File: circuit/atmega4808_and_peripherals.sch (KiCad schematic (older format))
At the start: 30 parts, among them J3 Conn_01x04, J4 Conn_02x04_Top_Bottom, J5 Conn_02x04_Top_Bottom, Q1 BSS138, U10 ATmega4808-X, U7 SN65HVD72, U8 TC4424AVOA, U9 ESP32-WROOM-32

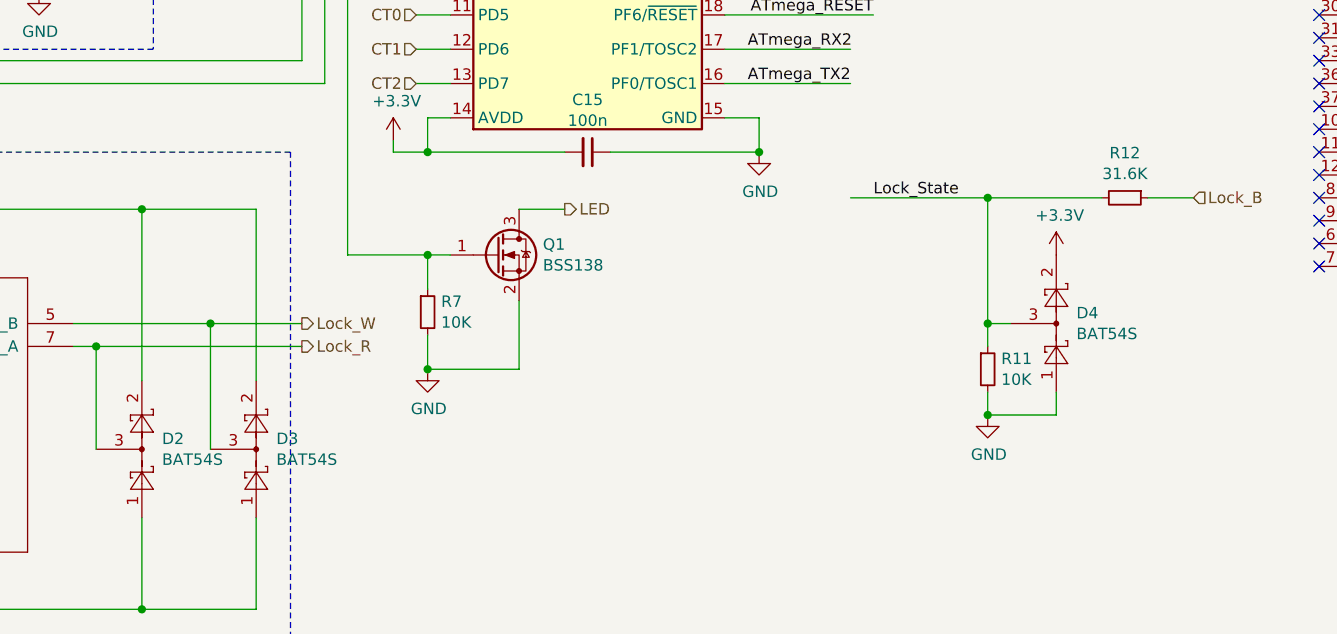
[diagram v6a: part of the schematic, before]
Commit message: Add new component data in schematic
Updated components and footprints in schematic
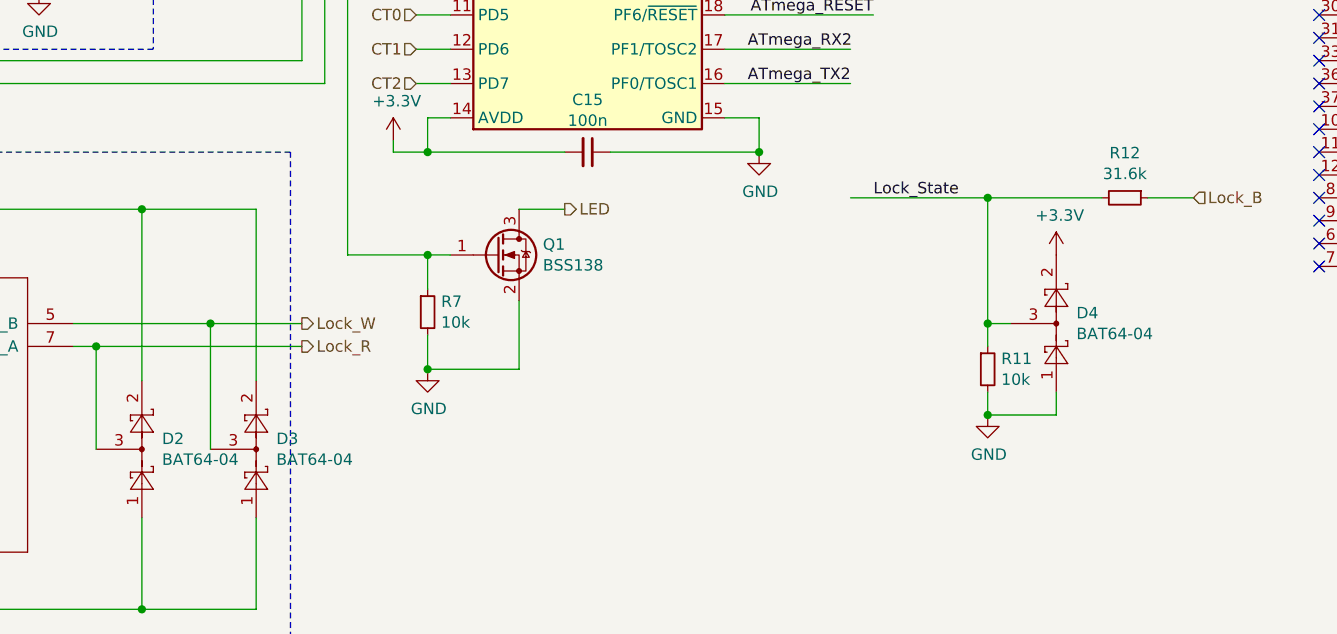
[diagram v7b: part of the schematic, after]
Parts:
- C12: footprint (none) -> Capacitor_THT:CP_Radial_D22.0mm_P10.00mm_SnapIn; Part (none) -> Yageo LG016M10K0BPF-2230 Elektrolyt-Kondensator SnapIn 10 m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; PartNo (none) -> 445516; Supplier (none) -> Conrad
- C13, C14, C15, C17: footprint (none) -> Capacitor_SMD:C_0603_1608Metric_Pad1.05x0.95mm_HandSolder; Part (none) -> Kemet C0603C104K3RAC7867+ Keramik-Kondensator SMD 0603 100 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; PartNo (none) -> 1420339; Supplier (none) -> Conrad
- C16: footprint (none) -> Capacitor_Tantalum_SMD:CP_EIA-7343-15_Kemet-W_Pad2.25x2.55mm_HandSolder; Part (none) -> Kemet T491D107K010AT Tantal-Kondensator SMD 100 µF 10 V 10 %; PartNo (none) -> 458352; Supplier (none) -> Conrad
- C21: footprint (none) -> Capacitor_SMD:C_0603_1608Metric_Pad1.05x0.95mm_HandSolder; Part (none) -> Thomsen Keramik-Kondensator SMD 0603 1 nF 50 V 10 %; PartNo (none) -> 454419; Supplier (none) -> Conrad
- C22: footprint (none) -> Capacitor_SMD:C_0603_1608Metric_Pad1.05x0.95mm_HandSolder; Part (none) -> Kemet C0603C105K4PAC7867+ Keramik-Kondensator SMD 0603 1 µF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; PartNo (none) -> 457925; Supplier (none) -> Conrad
- D2, D3, D4: value BAT54S -> BAT64-04; footprint Package_TO_SOT_SMD:SOT-23 -> Package_TO_SOT_SMD:SOT-23_Handsoldering; Part (none) -> Gleichrichter BAT64-04 (Dual) SOT-23-3 40 V Array - 1 Paar 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; PartNo (none) -> 152998; Supplier (none) -> Conrad
- J3: Part (none) -> BKL Electronic Stiftleiste (Standard) Anzahl Reihen: 1 Polz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; PartNo (none) -> 741146; Supplier (none) -> Conrad
- J4, J5: Part (none) -> econ connect SL8G2 Stiftleisten; PartNo (none) -> 801093043
- Q1: footprint (none) -> Package_TO_SOT_SMD:SOT-23_Handsoldering; Part (none) -> Infineon Technologies BSS138 MOSFET 1 N-Kanal 360 mW SOT-23; PartNo (none) -> 152928; Supplier (none) -> Conrad
- R10, R3, R4, R5, R6, R8, R9: footprint (none) -> Resistor_SMD:R_0603_1608Metric_Pad1.05x0.95mm_HandSolder; Part (none) -> TRU COMPONENTS TC-0603SAJ0101T5E203 Dickschicht-Widerstand 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; PartNo (none) -> 1583838; Supplier (none) -> Conrad
- R11, R7: value 10K -> 10k; footprint (none) -> Resistor_SMD:R_0603_1608Metric_Pad1.05x0.95mm_HandSolder; Part (none) -> TRU COMPONENTS TC-0603SAF1002T5E203 Dickschicht-Widerstand 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; PartNo (none) -> 1585269; Supplier (none) -> Conrad
- R12: value 31.6K -> 31.6k; footprint (none) -> Resistor_SMD:R_0603_1608Metric_Pad1.05x0.95mm_HandSolder; Part (none) -> TRU COMPONENTS TC-0603SAJ0303T5E203 Dickschicht-Widerstand 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; PartNo (none) -> 1584281; Supplier (none) -> Conrad
- R25: footprint (none) -> Resistor_SMD:R_0603_1608Metric_Pad1.05x0.95mm_HandSolder; Part (none) -> TRU COMPONENTS TC-0603SAJ0123T5E203 Dickschicht-Widerstand 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; PartNo (none) -> 1585796; Supplier (none) -> Conrad

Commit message: Update Parts List with Mouser ordering info
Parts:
- C12: Part Yageo LG016M10K0BPF-2230 Elektrolyt-Kondensator SnapIn 10 m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 -> (none); PartNo 445516 -> (none); Supplier Conrad -> Mouser
- C13, C14, C15, C17: Part Kemet C0603C104K3RAC7867+ Keramik-Kondensator SMD 0603 100 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 -> (none); PartNo 1420339 -> (none); Supplier Conrad -> Mouser
- C16: Part Kemet T491D107K010AT Tantal-Kondensator SMD 100 µF 10 V 10 % -> (none); PartNo 458352 -> (none); Supplier Conrad -> Mouser
- C21: Part Thomsen Keramik-Kondensator SMD 0603 1 nF 50 V 10 % -> (none); PartNo 454419 -> (none); Supplier Conrad -> Mouser
- C22: Part Kemet C0603C105K4PAC7867+ Keramik-Kondensator SMD 0603 1 µF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 -> (none); PartNo 457925 -> (none); Supplier Conrad -> Mouser
- D2, D3, D4: value BAT64-04 -> BAT54S; Part Gleichrichter BAT64-04 (Dual) SOT-23-3 40 V Array - 1 Paar 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 -> (none); PartNo 152998 -> 583-BAT54S; Supplier Conrad -> Mouser
- J3: Part BKL Electronic Stiftleiste (Standard) Anzahl Reihen: 1 Polz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 -> (none); PartNo 741146 -> 710-61304011121; Supplier Conrad -> Mouser
- J4, J5: Part econ connect SL8G2 Stiftleisten -> (none); PartNo 801093043 -> 710-61300821121; Supplier (none) -> Mouser
- Q1: Part Infineon Technologies BSS138 MOSFET 1 N-Kanal 360 mW SOT-23 -> (none); PartNo 152928 -> 512-BSS138; Supplier Conrad -> Mouser
- R10, R3, R4, R5, R6, R8, R9: Part TRU COMPONENTS TC-0603SAJ0101T5E203 Dickschicht-Widerstand 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 -> (none); PartNo 1583838 -> 594-MCT06030C1000FP5; Supplier Conrad -> Mouser
- R11, R7: Part TRU COMPONENTS TC-0603SAF1002T5E203 Dickschicht-Widerstand 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 -> (none); PartNo 1585269 -> 594-MCT06030C1002FP5; Supplier Conrad -> Mouser
- R12: Part TRU COMPONENTS TC-0603SAJ0303T5E203 Dickschicht-Widerstand 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 -> (none); PartNo 1584281 -> 594-MCT06030C3162FP5; Supplier Conrad -> Mouser
- R25: Part TRU COMPONENTS TC-0603SAJ0123T5E203 Dickschicht-Widerstand 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 -> (none); PartNo 1585796 -> 594-MCT06030C1202FP5; Supplier Conrad -> Mouser
- U10, U9: Supplier (none) -> Mouser
- U7: value SN65HVD72 -> SN65HVD72C; footprint (none) -> Package_SO:SOIC-8_3.9x4.9mm_P1.27mm; symbol smartevse:SN65HVD72 -> smartevse:SN65HVD72C; Supplier (none) -> Mouser
- U8: value TC4424AVOA -> FAN3214TMX; footprint (none) -> Package_SO:SOIC-8_3.9x4.9mm_P1.27mm; symbol smartevse:TC4424AVOA -> smartevse:FAN3214TMX; Supplier (none) -> Mouser
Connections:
- net labels added: Signal_Relay
- net labels removed: Reed_Relay
